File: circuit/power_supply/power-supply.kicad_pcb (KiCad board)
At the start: 2 copper layers, 16 parts, among them U1 MCS34063A

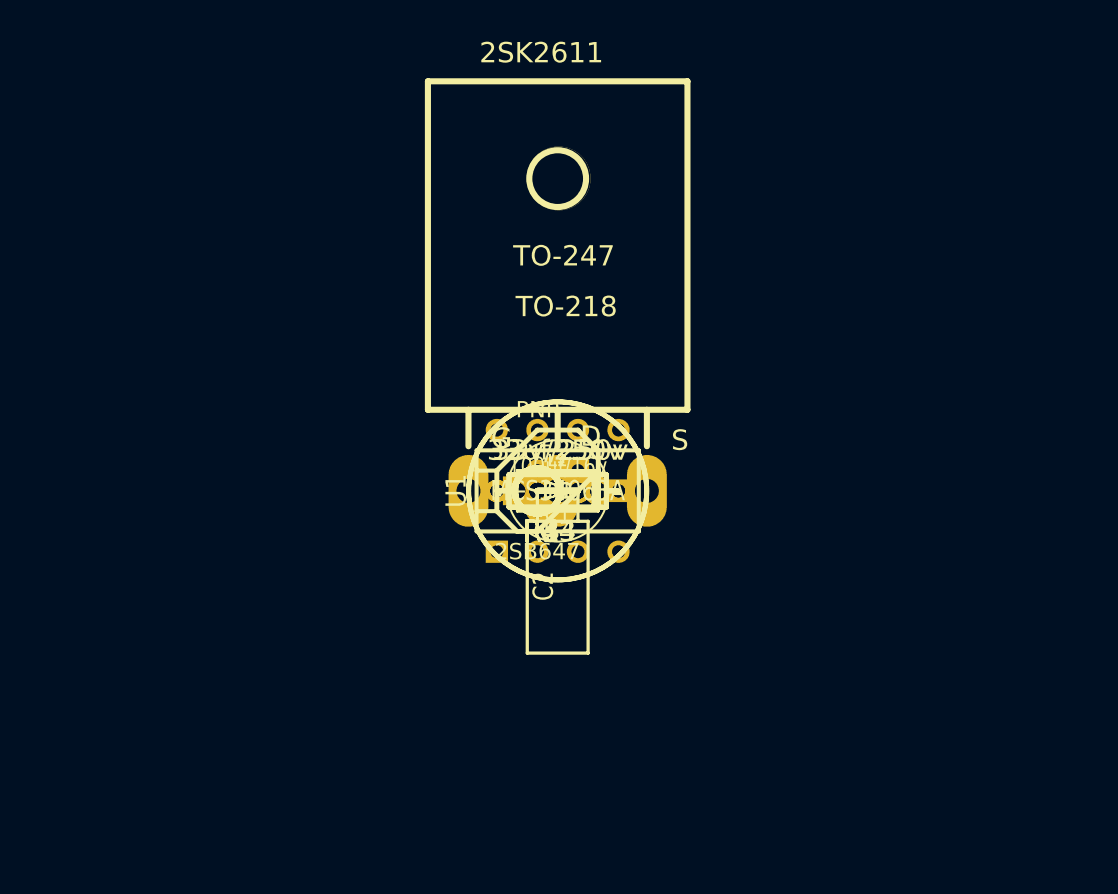
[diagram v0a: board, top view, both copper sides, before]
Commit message: power_supply: completed the nixie tube power supply circuit
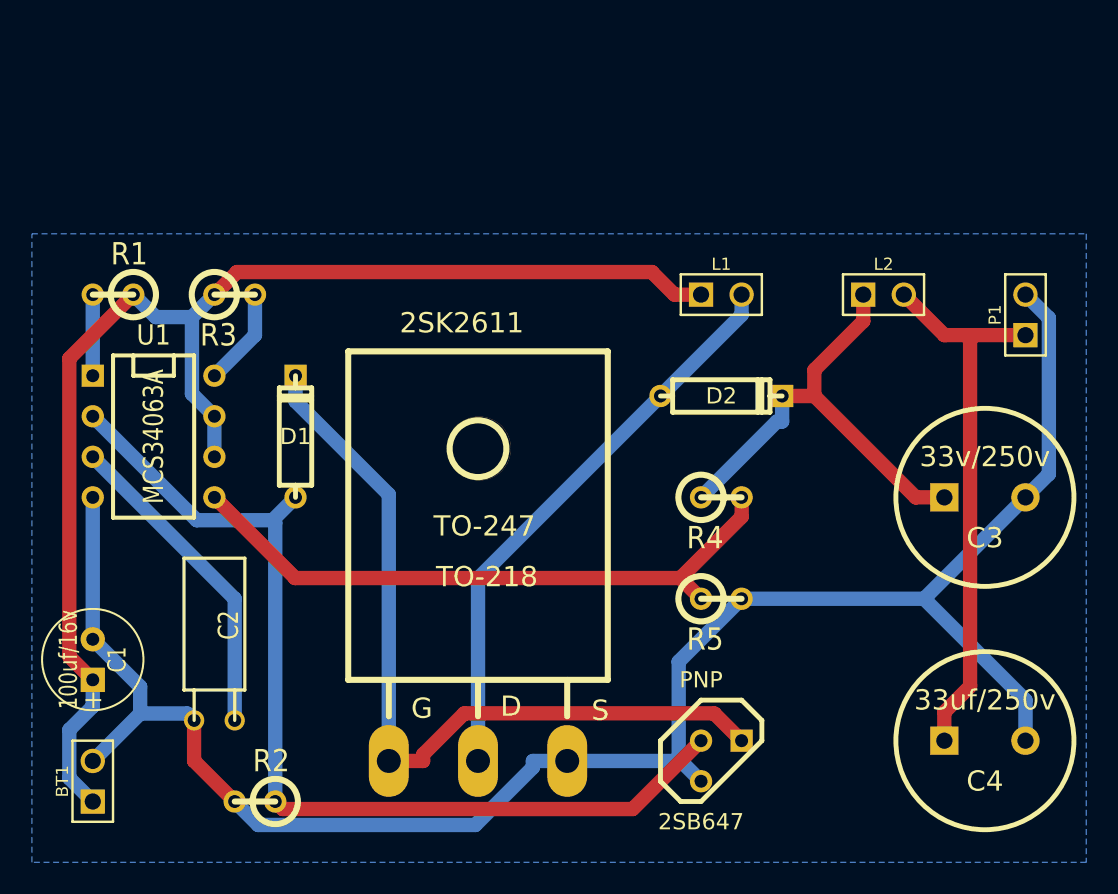
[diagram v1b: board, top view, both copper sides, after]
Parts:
- added BT1: BATTERY, PIN_ARRAY_2X1, F.Cu at (119.4, 123.2)
- added P1: CONN_2, PIN_ARRAY_2X1, F.Cu at (177.8, 94.0)
- moved C4 31.0 mm to (175.3, 120.7)
- moved C1 31.0 mm to (119.4, 115.6), turned to 90 degrees
- moved R1 30.4 mm to (120.7, 92.7), turned to 180 degrees
- moved R2 27.2 mm to (129.5, 124.5), turned to 180 degrees
- moved C3 26.8 mm to (175.3, 105.4)
- moved C2 25.9 mm to (127.0, 119.4), turned to 180 degrees
- moved U1 25.5 mm to (123.2, 101.6), turned to 270 degrees
- moved L2 23.8 mm to (168.9, 92.7)
- moved R3 23.7 mm to (128.3, 92.7)
- moved 2SB647 19.8 mm to (158.8, 121.9)
- moved 2SK2611 17.6 mm to (143.5, 121.9)
- moved D1 16.8 mm to (132.1, 101.6), turned to 90 degrees
- moved L1 16.0 mm to (158.8, 92.7)
- moved R5 12.3 mm to (158.8, 111.8)
- moved D2 11.8 mm to (158.8, 99.1)
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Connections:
- net +12V renamed N-0000010
- net +170V renamed N-000006
- net GNDPWR renamed N-000008
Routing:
- net N-000008: track 0.00 -> 118.5 mm
- net N-0000010: track 0.00 -> 82.5 mm
- net N-000009: track 0.00 -> 62.3 mm
- net N-000004: track 0.00 -> 50.8 mm
- net N-000005: track 0.00 -> 39.8 mm
- net N-000001: track 0.00 -> 36.0 mm
- net N-000006: track 0.00 -> 34.7 mm
- net N-000003: track 0.00 -> 29.1 mm
- net N-0000011: track 0.00 -> 20.2 mm
- net N-000002: track 0.00 -> 6.13 mm
- net N-000007: track 0.00 -> 5.08 mm
- added copper zone on B.Cu, net (none)
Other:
- net class Default: trace_width 0.254 -> 0.9

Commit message: power_supply: increased the size of the track line
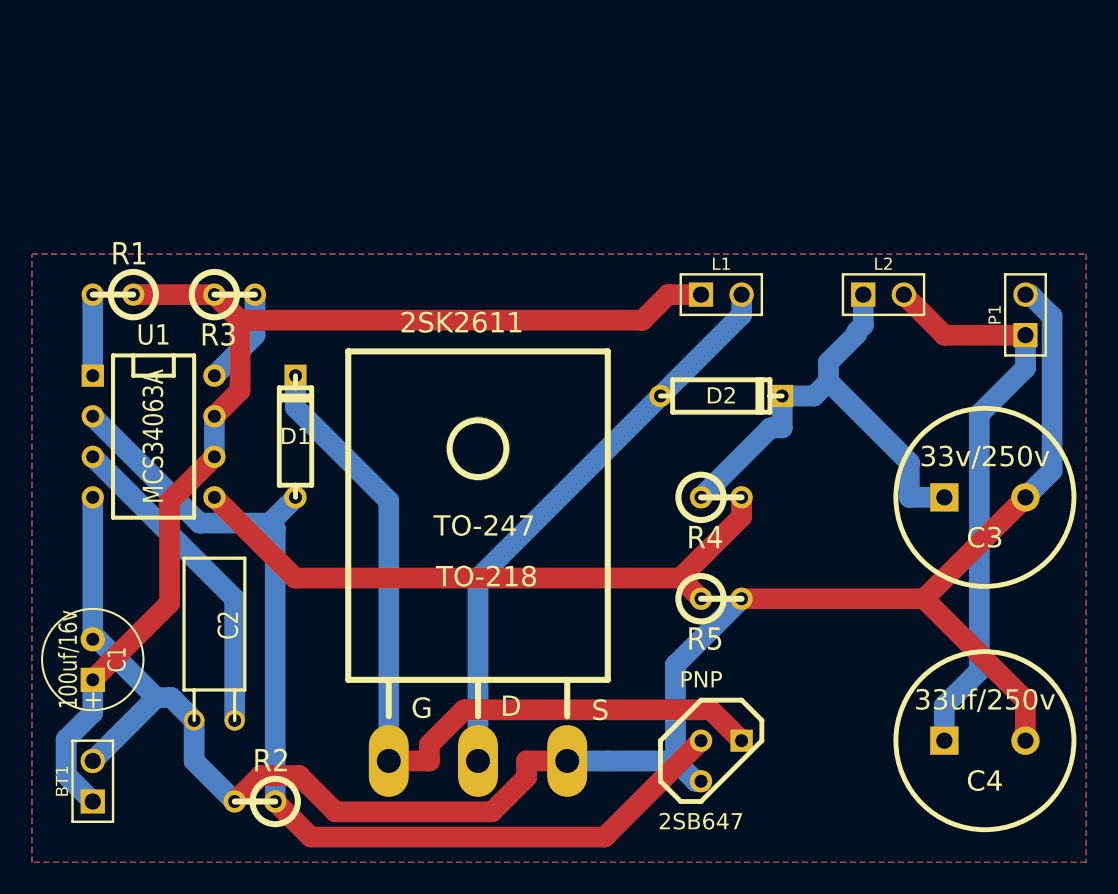
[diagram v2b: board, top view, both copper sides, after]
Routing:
- net N-0000010: track 82.5 -> 72.2 mm
- net N-000008: track 118.5 -> 120.4 mm
- net N-000009: track 62.3 -> 63.8 mm
- net N-000006: track 34.7 -> 36.2 mm
- net N-000003: track 29.1 -> 30.0 mm
- net N-000004: track 50.8 -> 51.4 mm
- added copper zone on F.Cu, net (none)
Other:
- net class Default: trace_width 0.9 -> 1.3

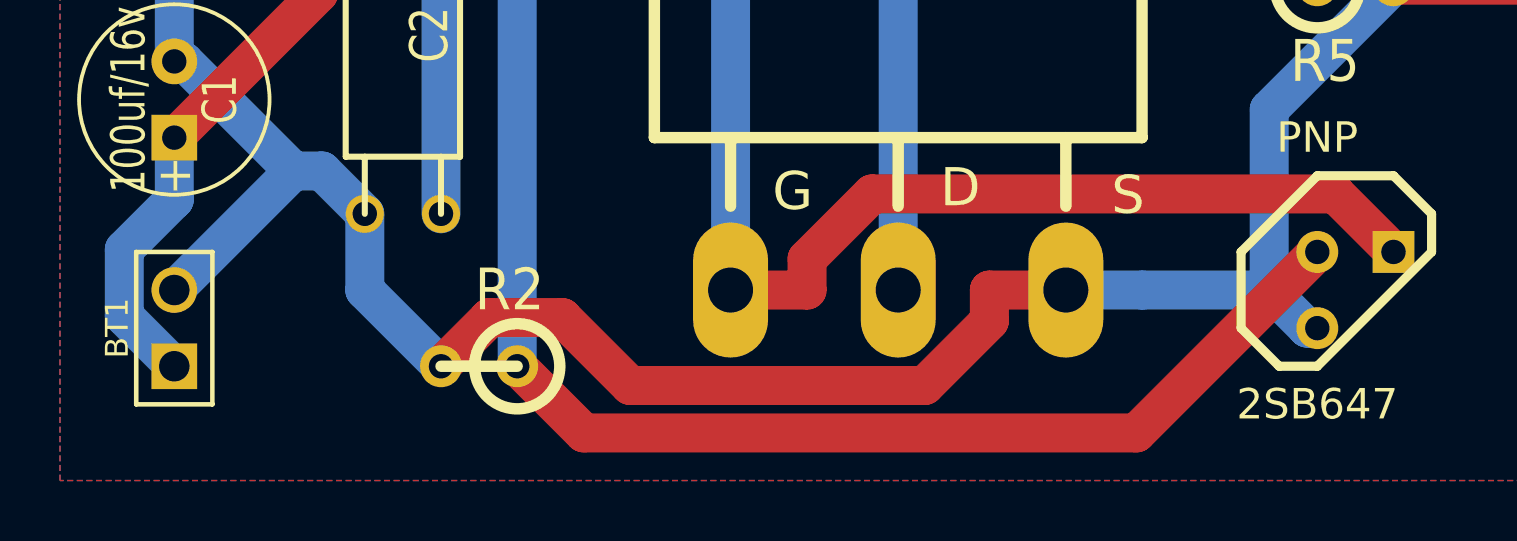
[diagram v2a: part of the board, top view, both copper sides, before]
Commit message: power_supply: added some space between two track lines
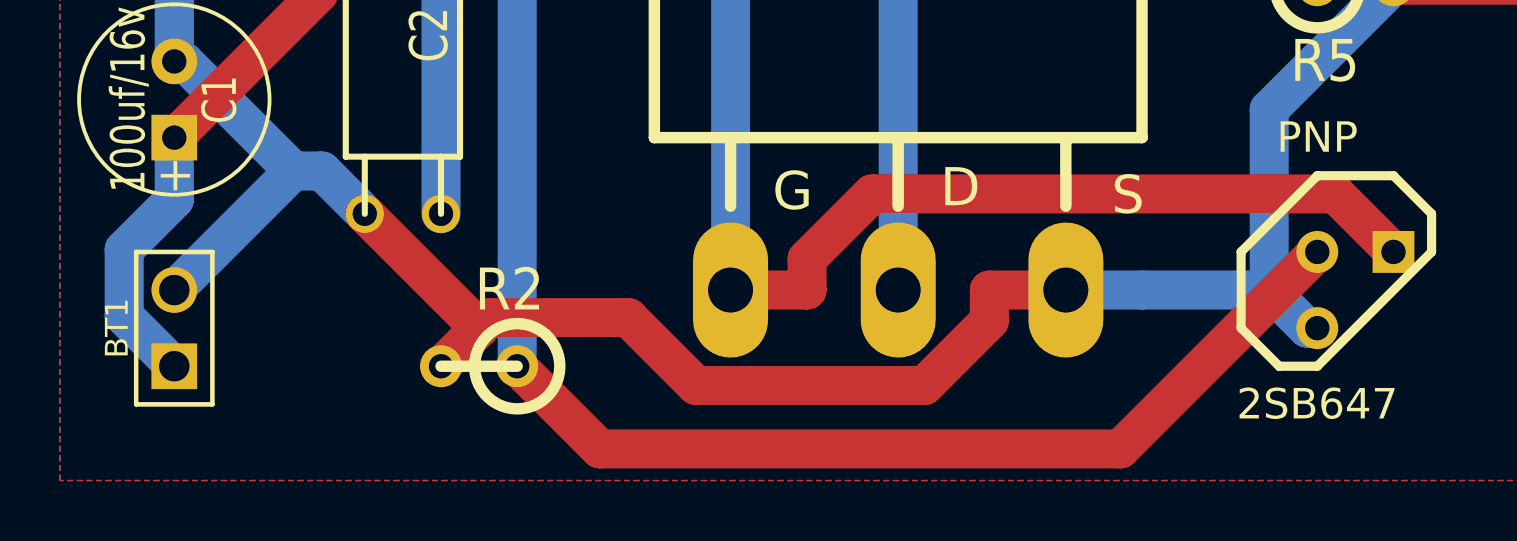
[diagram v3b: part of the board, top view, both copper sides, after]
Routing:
- net N-000008: track 120.4 -> 119.7 mm
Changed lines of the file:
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@@
   (segment (start 154.94 99.06) (end 143.51 110.49) (width 1.3) (layer B.Cu) (net 1))
   (segment (start 127 100.33) (end 127 102.87) (width 1.3) (layer B.Cu) (net 2))
-  (segment (start 117.7136 120.5684) (end 119.38 118.902) (width 1.3) (layer B.Cu) (net 2))
-  (segment (start 117.7136 122.7936) (end 117.7136 120.5684) (width 1.3) (layer B.Cu) (net 2))
-  (segment (start 119.38 124.46) (end 117.7136 122.7936) (width 1.3) (layer B.Cu) (net 2))
-  (segment (start 119.38 116.84) (end 119.38 118.902) (width 1.3) (layer B.Cu) (net 2))
   (segment (start 157.48 92.71) (end 155.418 92.71) (width 1.3) (layer F.Cu) (net 2))
   (segment (start 127 92.71) (end 121.92 92.71) (width 1.3) (layer F.Cu) (net 2))
@@
   (segment (start 153.8134 94.3146) (end 155.418 92.71) (width 1.3) (layer F.Cu) (net 2))
   (segment (start 128.6046 94.3146) (end 153.8134 94.3146) (width 1.3) (layer F.Cu) (net 2))
+  (segment (start 117.7071 122.7871) (end 119.38 124.46) (width 1.3) (layer B.Cu) (net 2))
+  (segment (start 117.7071 120.5749) (end 117.7071 122.7871) (width 1.3) (layer B.Cu) (net 2))
+  (segment (start 119.38 118.902) (end 117.7071 120.5749) (width 1.3) (layer B.Cu) (net 2))
+  (segment (start 119.38 116.84) (end 119.38 118.902) (width 1.3) (layer B.Cu) (net 2))
   (segment (start 128.27 111.76) (end 128.27 119.38) (width 1.3) (layer B.Cu) (net 3))
   (segment (start 119.38 102.87) (end 128.27 111.76) (width 1.3) (layer B.Cu) (net 3))
@@
   (segment (start 119.38 97.79) (end 119.38 92.71) (width 1.3) (layer B.Cu) (net 9))
   (segment (start 119.38 105.41) (end 119.38 114.3) (width 1.3) (layer B.Cu) (net 10))
-  (segment (start 125.73 121.92) (end 125.73 119.38) (width 1.3) (layer B.Cu) (net 10))
-  (segment (start 128.27 124.46) (end 125.73 121.92) (width 1.3) (layer B.Cu) (net 10))
   (segment (start 119.6975 114.3) (end 123.3488 117.9512) (width 1.3) (layer B.Cu) (net 10))
   (segment (start 119.38 114.3) (end 119.6975 114.3) (width 1.3) (layer B.Cu) (net 10))
@@
   (segment (start 125.73 119.38) (end 124.3012 117.9512) (width 1.3) (layer B.Cu) (net 10))
   (segment (start 123.3488 117.9512) (end 119.38 121.92) (width 1.3) (layer B.Cu) (net 10))
-  (segment (start 146.5483 122.9485) (end 146.5483 121.92) (width 1.3) (layer F.Cu) (net 10))
-  (segment (start 144.3948 125.102) (end 146.5483 122.9485) (width 1.3) (layer F.Cu) (net 10))
-  (segment (start 134.5763 125.102) (end 144.3948 125.102) (width 1.3) (layer F.Cu) (net 10))
-  (segment (start 132.3128 122.8385) (end 134.5763 125.102) (width 1.3) (layer F.Cu) (net 10))
-  (segment (start 129.8915 122.8385) (end 132.3128 122.8385) (width 1.3) (layer F.Cu) (net 10))
-  (segment (start 128.27 124.46) (end 129.8915 122.8385) (width 1.3) (layer F.Cu) (net 10))
   (segment (start 149.098 121.92) (end 146.5483 121.92) (width 1.3) (layer F.Cu) (net 10))
   (segment (start 178.0974 92.71) (end 177.8 92.71) (width 1.3) (layer B.Cu) (net 10))
   (segment (start 179.4664 94.079) (end 178.0974 92.71) (width 1.3) (layer B.Cu) (net 10))
   (segment (start 179.4664 103.7436) (end 179.4664 94.079) (width 1.3) (layer B.Cu) (net 10))
-  (segment (start 177.8 105.41) (end 179.4664 103.7436) (width 1.3) (layer B.Cu) (net 10) (status 400000))
+  (segment (start 177.8 105.41) (end 179.4664 103.7436) (width 1.3) (layer B.Cu) (net 10))
   (segment (start 149.098 121.92) (end 151.6477 121.92) (width 1.3) (layer B.Cu) (net 10))
   (segment (start 151.6477 121.92) (end 155.8771 121.92) (width 1.3) (layer B.Cu) (net 10))
@@
   (segment (start 177.8 105.41) (end 171.45 111.76) (width 1.3) (layer F.Cu) (net 10))
   (segment (start 171.45 111.76) (end 160.02 111.76) (width 1.3) (layer F.Cu) (net 10))
+  (segment (start 125.73 119.38) (end 129.54 123.19) (width 1.3) (layer F.Cu) (net 10))
+  (segment (start 129.54 123.19) (end 128.27 124.46) (width 1.3) (layer F.Cu) (net 10))
+  (segment (start 129.8927 122.8373) (end 129.54 123.19) (width 1.3) (layer F.Cu) (net 10))
+  (segment (start 134.5096 122.8373) (end 129.8927 122.8373) (width 1.3) (layer F.Cu) (net 10))
+  (segment (start 136.7743 125.102) (end 134.5096 122.8373) (width 1.3) (layer F.Cu) (net 10))
+  (segment (start 144.3873 125.102) (end 136.7743 125.102) (width 1.3) (layer F.Cu) (net 10))
+  (segment (start 146.5483 122.941) (end 144.3873 125.102) (width 1.3) (layer F.Cu) (net 10))
+  (segment (start 146.5483 121.92) (end 146.5483 122.941) (width 1.3) (layer F.Cu) (net 10))
   (segment (start 130.81 107.3598) (end 130.4701 107.0199) (width 1.3) (layer B.Cu) (net 11))
   (segment (start 130.81 124.46) (end 130.81 107.3598) (width 1.3) (layer B.Cu) (net 11))
@@
   (segment (start 119.38 100.33) (end 126.0699 107.0199) (width 1.3) (layer B.Cu) (net 11))
   (segment (start 130.4701 107.0199) (end 132.08 105.41) (width 1.3) (layer B.Cu) (net 11))
-  (segment (start 151.4465 126.6835) (end 157.48 120.65) (width 1.3) (layer F.Cu) (net 11))
-  (segment (start 133.0335 126.6835) (end 151.4465 126.6835) (width 1.3) (layer F.Cu) (net 11))
-  (segment (start 130.81 124.46) (end 133.0335 126.6835) (width 1.3) (layer F.Cu) (net 11))
+  (segment (start 150.9139 127.2161) (end 157.48 120.65) (width 1.3) (layer F.Cu) (net 11))
+  (segment (start 133.5661 127.2161) (end 150.9139 127.2161) (width 1.3) (layer F.Cu) (net 11))
+  (segment (start 130.81 124.46) (end 133.5661 127.2161) (width 1.3) (layer F.Cu) (net 11))
   (zone (net 0) (net_name "") (layer B.Cu) (hatch edge 0.508)
     (connect_pads (clearance 1))

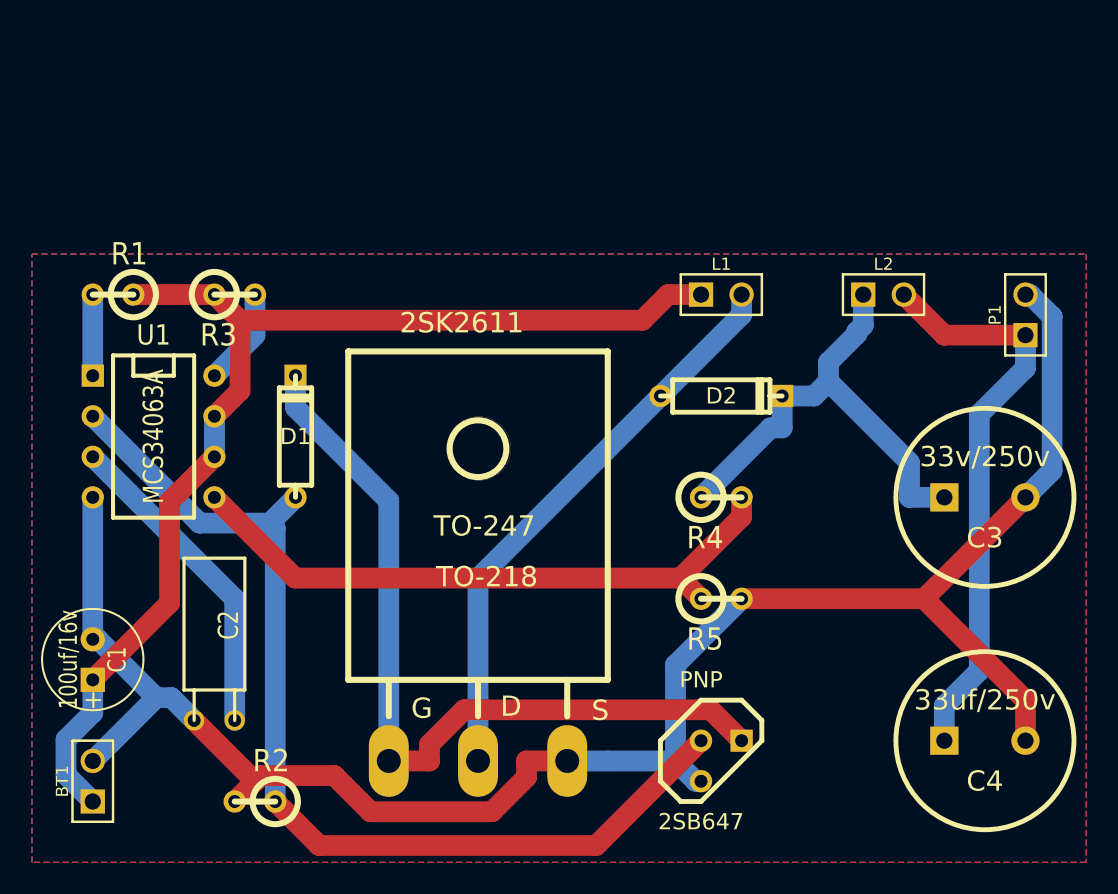
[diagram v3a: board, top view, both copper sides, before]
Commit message: power_supply: added two resistors into the circuit
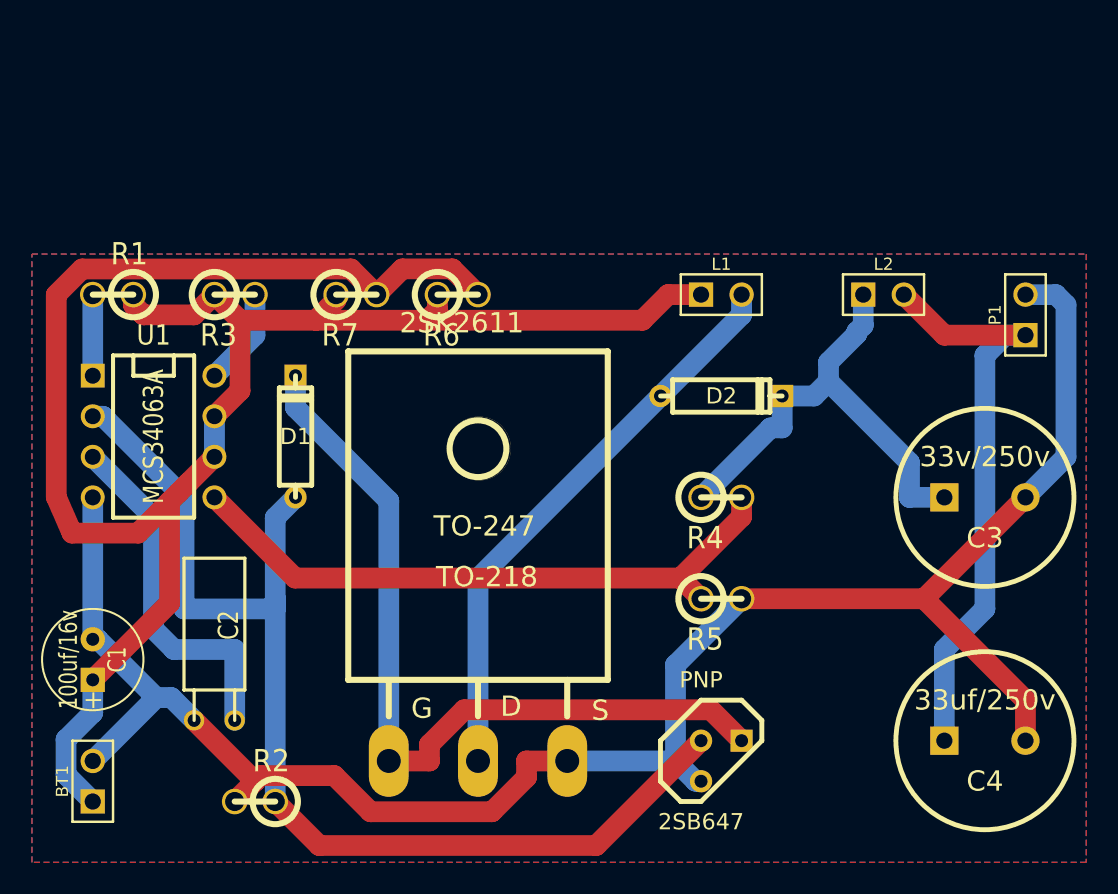
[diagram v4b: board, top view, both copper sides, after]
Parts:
- added R6: 0.5 ohm, R1, F.Cu at (142.2, 92.7)
- added R7: 0.5 ohm, R1, F.Cu at (135.9, 92.7)
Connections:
- BT1 pad 1: N-0000010 (its old number) -> N-0000011
- C1 pad 1: N-0000010 (its old number) -> N-0000011
- L1 pad 1: N-0000010 (its old number) -> N-000009
- R1 pad 1: N-0000010 (its old number) -> N-000009
- R3 pad 1: N-0000010 (its old number) -> N-000009
- U1 pad 6: N-0000010 (its old number) -> N-0000011
- U1 pad 7: N-0000010 (its old number) -> N-000009
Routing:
- net N-0000011: track 0.00 -> 77.3 mm
- net N-0000010 (its old number): track 72.2 -> 0.00 mm
- net N-000009: track 0.00 -> 51.5 mm
- net N-000008: track 64.3 -> 71.9 mm
- net N-0000012: track 20.2 -> 22.4 mm
- net N-000007: track 119.7 -> 121.3 mm
- net N-000005: track 36.2 -> 36.9 mm

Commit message: power_supply: imported the OSHW logo and adjusted the route
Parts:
- added OSHW_COPPER_10MM: VAL**, OSHW_COPPER_10MM, F.Cu at (165.7, 123.8)
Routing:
- net N-0000011: track 77.3 -> 80.2 mm
- net N-000007: track 121.3 -> 124.2 mm
- net N-000009: track 51.5 -> 52.4 mm
- net N-000002: track 30.0 -> 30.7 mm
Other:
- board text added: "2014.2.4"
